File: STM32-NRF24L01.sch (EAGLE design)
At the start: 16 parts, among them IC1 STM32F030K6T6, IC2 MCP73811/2, J1 61301411121, J2 61301411121, P1 PUSH-SMD

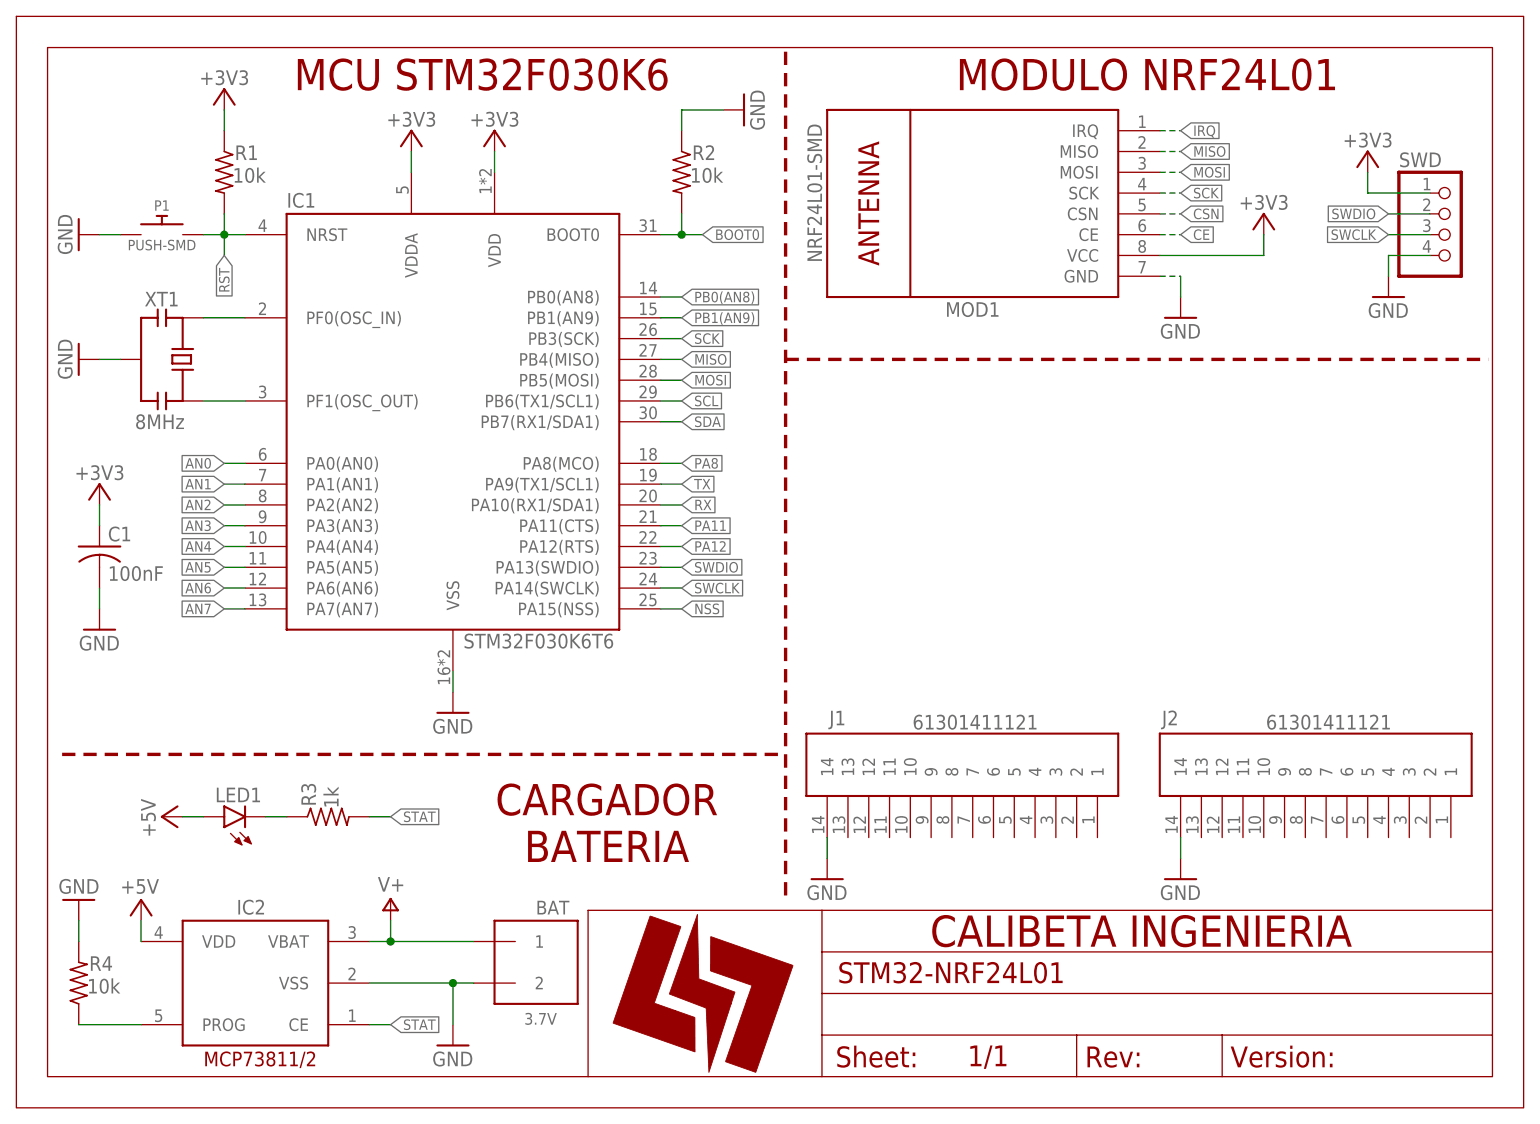
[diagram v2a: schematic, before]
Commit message: Add Regulador 3V3
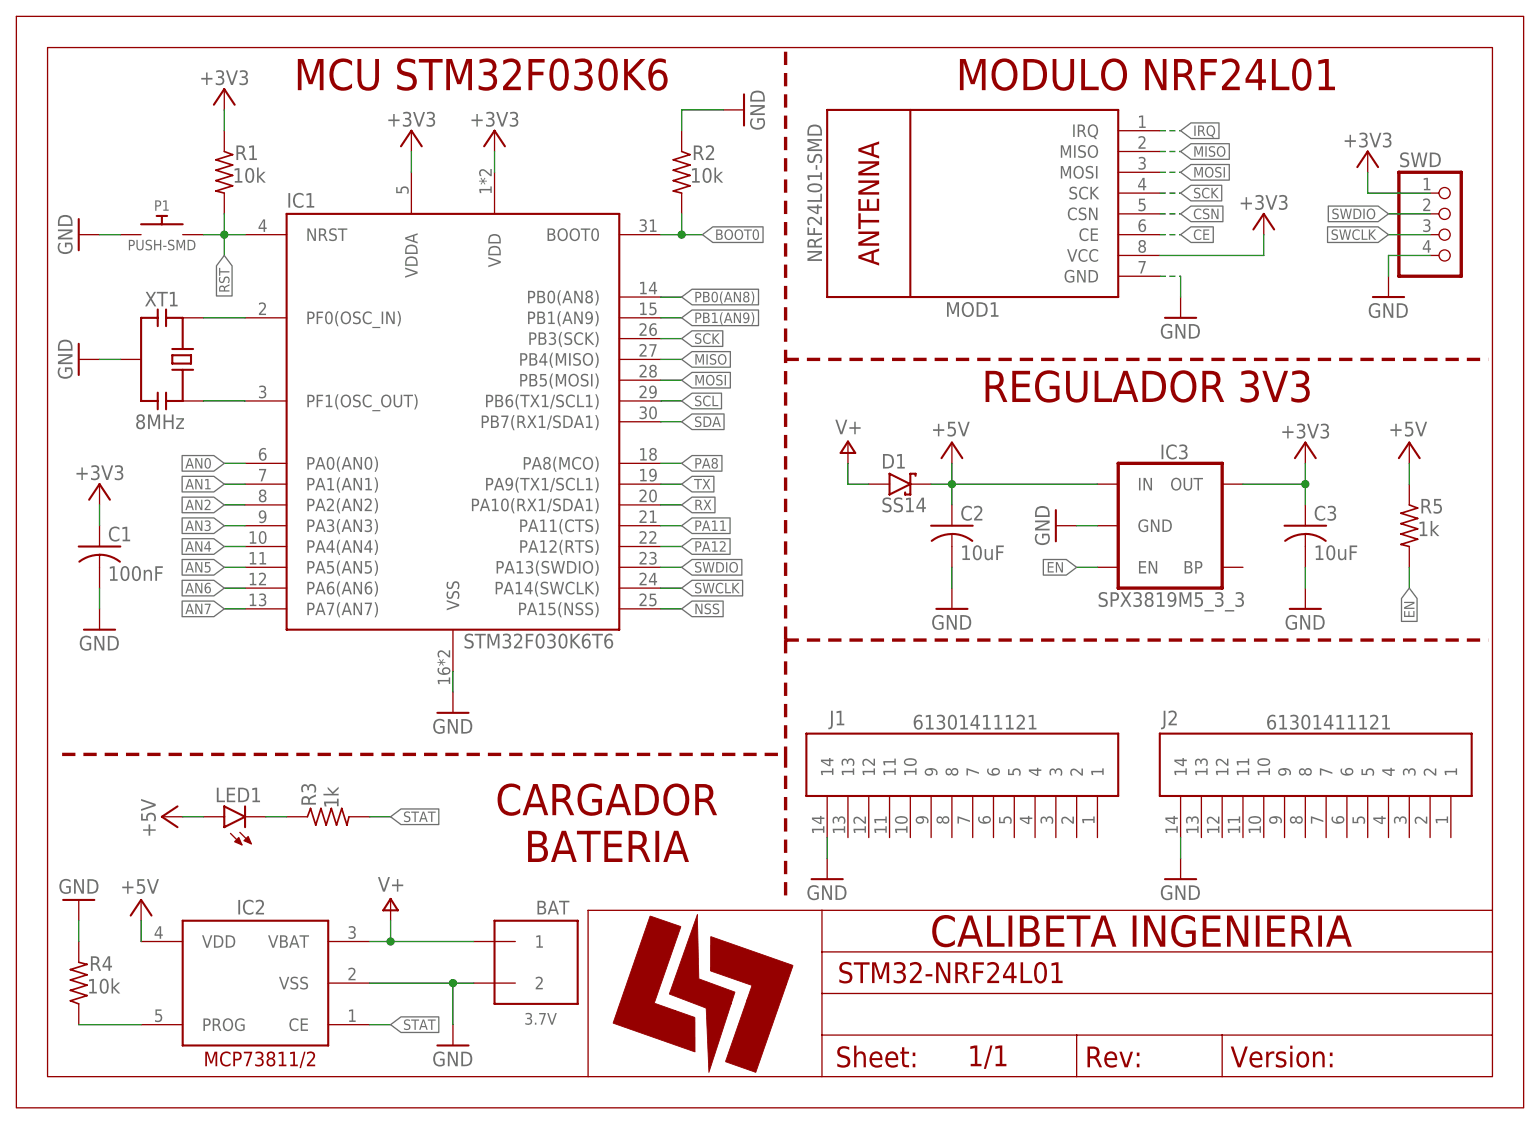
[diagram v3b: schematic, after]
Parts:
- added C2, C3: 10uF, CaliBeta-RCL:CAPC0805
- added D1: SS14, CaliBeta-Diodos:SS14
- added IC3: SPX3819M5_3_3, SparkFun-IC-Power:V_REG_SPX3819-SOT23-5
- added R5: 1k, CaliBeta-RCL:RESISTOR_R0805
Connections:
- new net EN: IC3.EN, R5.2
- net +3V3: now also C3.1, IC3.OUT
- net +5V: now also C2.1, D1.K, IC3.IN, R5.1
- net GND: now also C2.2, C3.2, IC3.GND
- net V+: now also D1.A
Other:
- note added: "REGULADOR 3V3"
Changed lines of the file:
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@@
 <part name="P+3" library="supply1" library_urn="urn:adsk.eagle:library:371" deviceset="V+" device=""/>
 <part name="GND10" library="supply1" library_urn="urn:adsk.eagle:library:371" deviceset="GND" device=""/>
+<part name="IC3" library="SparkFun-IC-Power" library_urn="urn:adsk.eagle:library:526" deviceset="V_REG_SPX3819" device="-SOT23-5" package3d_urn="urn:adsk.eagle:package:39060/1" value="SPX3819M5_3_3"/>
+<part name="D1" library="CaliBeta-Diodos" library_urn="urn:adsk.eagle:library:14345451" deviceset="SS14" device="" package3d_urn="urn:adsk.eagle:package:14345492/2"/>
+<part name="P+4" library="supply1" library_urn="urn:adsk.eagle:library:371" deviceset="V+" device=""/>
+<part name="P+5" library="supply1" library_urn="urn:adsk.eagle:library:371" deviceset="+5V" device=""/>
+<part name="C2" library="CaliBeta-RCL" library_urn="urn:adsk.eagle:library:14345719" deviceset="CAP" device="C0805" package3d_urn="urn:adsk.eagle:package:14345754/1" value="10uF"/>
+<part name="GND12" library="supply1" library_urn="urn:adsk.eagle:library:371" deviceset="GND" device=""/>
+<part name="+3V7" library="supply1" library_urn="urn:adsk.eagle:library:371" deviceset="+3V3" device=""/>
+<part name="C3" library="CaliBeta-RCL" library_urn="urn:adsk.eagle:library:14345719" deviceset="CAP" device="C0805" package3d_urn="urn:adsk.eagle:package:14345754/1" value="10uF"/>
+<part name="GND13" library="supply1" library_urn="urn:adsk.eagle:library:371" deviceset="GND" device=""/>
+<part name="GND14" library="supply1" library_urn="urn:adsk.eagle:library:371" deviceset="GND" device=""/>
+<part name="R5" library="CaliBeta-RCL" library_urn="urn:adsk.eagle:library:14345719" deviceset="RESISTOR_" device="R0805" package3d_urn="urn:adsk.eagle:package:14345749/1" value="1k"/>
+<part name="P+6" library="supply1" library_urn="urn:adsk.eagle:library:371" deviceset="+5V" device=""/>
 </parts>
 <sheets>
@@
 <plain>
 <text x="56.896" y="126.238" size="3.81" layer="94" ratio="10" align="center">MCU STM32F030K6</text>
-<wire x1="93.98" y1="129.032" x2="93.98" y2="43.18" width="0.4064" layer="94" style="longdash"/>
+<wire x1="93.98" y1="129.032" x2="93.98" y2="57.15" width="0.4064" layer="94" style="longdash"/>
 <text x="138.176" y="126.238" size="3.81" layer="94" ratio="10" align="center">MODULO NRF24L01</text>
+<wire x1="93.98" y1="57.15" x2="93.98" y2="43.18" width="0.4064" layer="94" style="longdash"/>
 <wire x1="93.98" y1="43.18" x2="93.98" y2="25.4" width="0.4064" layer="94" style="longdash"/>
 <wire x1="5.588" y1="43.18" x2="93.98" y2="43.18" width="0.4064" layer="94" style="longdash"/>
@@
 <text x="72.136" y="34.798" size="3.81" layer="94" ratio="10" align="center">CARGADOR
 BATERIA</text>
+<text x="138.176" y="88.138" size="3.81" layer="94" ratio="10" align="center">REGULADOR 3V3</text>
+<wire x1="93.98" y1="57.15" x2="179.832" y2="57.15" width="0.4064" layer="94" style="longdash"/>
 </plain>
 <instances>
@@
 <attribute name="VALUE" x="50.8" y="5.08" size="1.778" layer="96"/>
 </instance>
+<instance part="IC3" gate="G$1" x="142.24" y="71.12" smashed="yes">
+<attribute name="NAME" x="139.7" y="79.248" size="1.778" layer="95" font="vector"/>
+<attribute name="VALUE" x="132.08" y="62.992" size="1.778" layer="96" font="vector" align="top-left"/>
+</instance>
+<instance part="D1" gate="G$1" x="106.68" y="76.2" smashed="yes">
+<attribute name="NAME" x="105.664" y="78.105" size="1.778" layer="95"/>
+<attribute name="VALUE" x="105.664" y="72.771" size="1.778" layer="96"/>
+</instance>
+<instance part="P+4" gate="1" x="101.6" y="81.28" smashed="yes">
+<attribute name="VALUE" x="103.378" y="84.074" size="1.778" layer="96" rot="R180"/>
+</instance>
+<instance part="P+5" gate="1" x="114.3" y="81.28" smashed="yes">
+<attribute name="VALUE" x="111.76" y="82.042" size="1.778" layer="96"/>
+</instance>
+<instance part="C2" gate="G$1" x="114.3" y="71.12" smashed="yes">
+<attribute name="NAME" x="115.316" y="71.755" size="1.778" layer="95"/>
+<attribute name="VALUE" x="115.316" y="66.929" size="1.778" layer="96"/>
+</instance>
+<instance part="GND12" gate="1" x="114.3" y="60.96" smashed="yes">
+<attribute name="VALUE" x="111.76" y="58.42" size="1.778" layer="96"/>
+</instance>
+<instance part="+3V7" gate="G$1" x="157.48" y="81.28" smashed="yes">
+<attribute name="VALUE" x="154.432" y="81.788" size="1.778" layer="96"/>
+</instance>
+<instance part="C3" gate="G$1" x="157.48" y="71.12" smashed="yes">
+<attribute name="NAME" x="158.496" y="71.755" size="1.778" layer="95"/>
+<attribute name="VALUE" x="158.496" y="66.929" size="1.778" layer="96"/>
+</instance>
+<instance part="GND13" gate="1" x="157.48" y="60.96" smashed="yes">
+<attribute name="VALUE" x="154.94" y="58.42" size="1.778" layer="96"/>
+</instance>
+<instance part="GND14" gate="1" x="127" y="71.12" smashed="yes" rot="R270">
+<attribute name="VALUE" x="124.46" y="73.66" size="1.778" layer="96" rot="R270"/>
+</instance>
+<instance part="R5" gate="G$1" x="170.18" y="71.12" smashed="yes" rot="R270">
+<attribute name="NAME" x="171.45" y="72.6186" size="1.778" layer="95"/>
+<attribute name="VALUE" x="171.196" y="69.85" size="1.778" layer="96"/>
+</instance>
+<instance part="P+6" gate="1" x="170.18" y="81.28" smashed="yes">
+<attribute name="VALUE" x="167.64" y="82.042" size="1.778" layer="96"/>
+</instance>
 </instances>
 <busses>
@@
 <wire x1="48.26" y1="114.3" x2="48.26" y2="116.84" width="0.1524" layer="91"/>
 <pinref part="+3V6" gate="G$1" pin="+3V3"/>
+</segment>
+<segment>
+<pinref part="+3V7" gate="G$1" pin="+3V3"/>
+<pinref part="IC3" gate="G$1" pin="OUT"/>
+<wire x1="157.48" y1="78.74" x2="157.48" y2="76.2" width="0.1524" layer="91"/>
+<wire x1="157.48" y1="76.2" x2="149.86" y2="76.2" width="0.1524" layer="91"/>
+<pinref part="C3" gate="G$1" pin="1"/>
+<wire x1="157.48" y1="73.66" x2="157.48" y2="76.2" width="0.1524" layer="91"/>
+<junction x="157.48" y="76.2"/>
 </segment>
 </net>
@@
 <junction x="53.34" y="15.24"/>
 </segment>
+<segment>
+<pinref part="C2" gate="G$1" pin="2"/>
+<pinref part="GND12" gate="1" pin="GND"/>
+<wire x1="114.3" y1="63.5" x2="114.3" y2="66.04" width="0.1524" layer="91"/>
+</segment>
+<segment>
+<pinref part="C3" gate="G$1" pin="2"/>
+<pinref part="GND13" gate="1" pin="GND"/>
+<wire x1="157.48" y1="63.5" x2="157.48" y2="66.04" width="0.1524" layer="91"/>
+</segment>
+<segment>
+<pinref part="IC3" gate="G$1" pin="GND"/>
+<pinref part="GND14" gate="1" pin="GND"/>
+<wire x1="129.54" y1="71.12" x2="132.08" y2="71.12" width="0.1524" layer="91"/>
+</segment>
 </net>
 <net name="CE" class="0">
@@
 <pinref part="P+1" gate="1" pin="+5V"/>
 <wire x1="20.32" y1="35.56" x2="22.86" y2="35.56" width="0.1524" layer="91"/>
+</segment>
+<segment>
+<pinref part="P+5" gate="1" pin="+5V"/>
+<pinref part="D1" gate="G$1" pin="K"/>
+<wire x1="114.3" y1="78.74" x2="114.3" y2="76.2" width="0.1524" layer="91"/>
+<wire x1="114.3" y1="76.2" x2="111.76" y2="76.2" width="0.1524" layer="91"/>
+<pinref part="IC3" gate="G$1" pin="IN"/>
+<wire x1="132.08" y1="76.2" x2="114.3" y2="76.2" width="0.1524" layer="91"/>
+<junction x="114.3" y="76.2"/>
+<pinref part="C2" gate="G$1" pin="1"/>
+<wire x1="114.3" y1="73.66" x2="114.3" y2="76.2" width="0.1524" layer="91"/>
+</segment>
+<segment>
+<pinref part="R5" gate="G$1" pin="1"/>
+<pinref part="P+6" gate="1" pin="+5V"/>
+<wire x1="170.18" y1="78.74" x2="170.18" y2="76.2" width="0.1524" layer="91"/>
 </segment>
 </net>
@@
 <junction x="45.72" y="20.32"/>
 </segment>
+<segment>
+<pinref part="D1" gate="G$1" pin="A"/>
+<pinref part="P+4" gate="1" pin="V+"/>
+<wire x1="104.14" y1="76.2" x2="101.6" y2="76.2" width="0.1524" layer="91"/>
+<wire x1="101.6" y1="76.2" x2="101.6" y2="78.74" width="0.1524" layer="91"/>
+</segment>
 </net>
 <net name="STAT" class="0">
@@
 </segment>
 </net>
+<net name="EN" class="0">
+<segment>
+<pinref part="IC3" gate="G$1" pin="EN"/>
+<wire x1="132.08" y1="66.04" x2="129.54" y2="66.04" width="0.1524" layer="91"/>
+<label x="129.54" y="66.04" size="1.27" layer="95" ratio="10" rot="R180" xref="yes"/>
+</segment>
+<segment>
+<pinref part="R5" gate="G$1" pin="2"/>
+<wire x1="170.18" y1="66.04" x2="170.18" y2="63.5" width="0.1524" layer="91"/>
+<label x="170.18" y="63.5" size="1.27" layer="95" ratio="10" rot="R270" xref="yes"/>
+</segment>
+</net>

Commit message: Terminado SCH, Inicio BRD
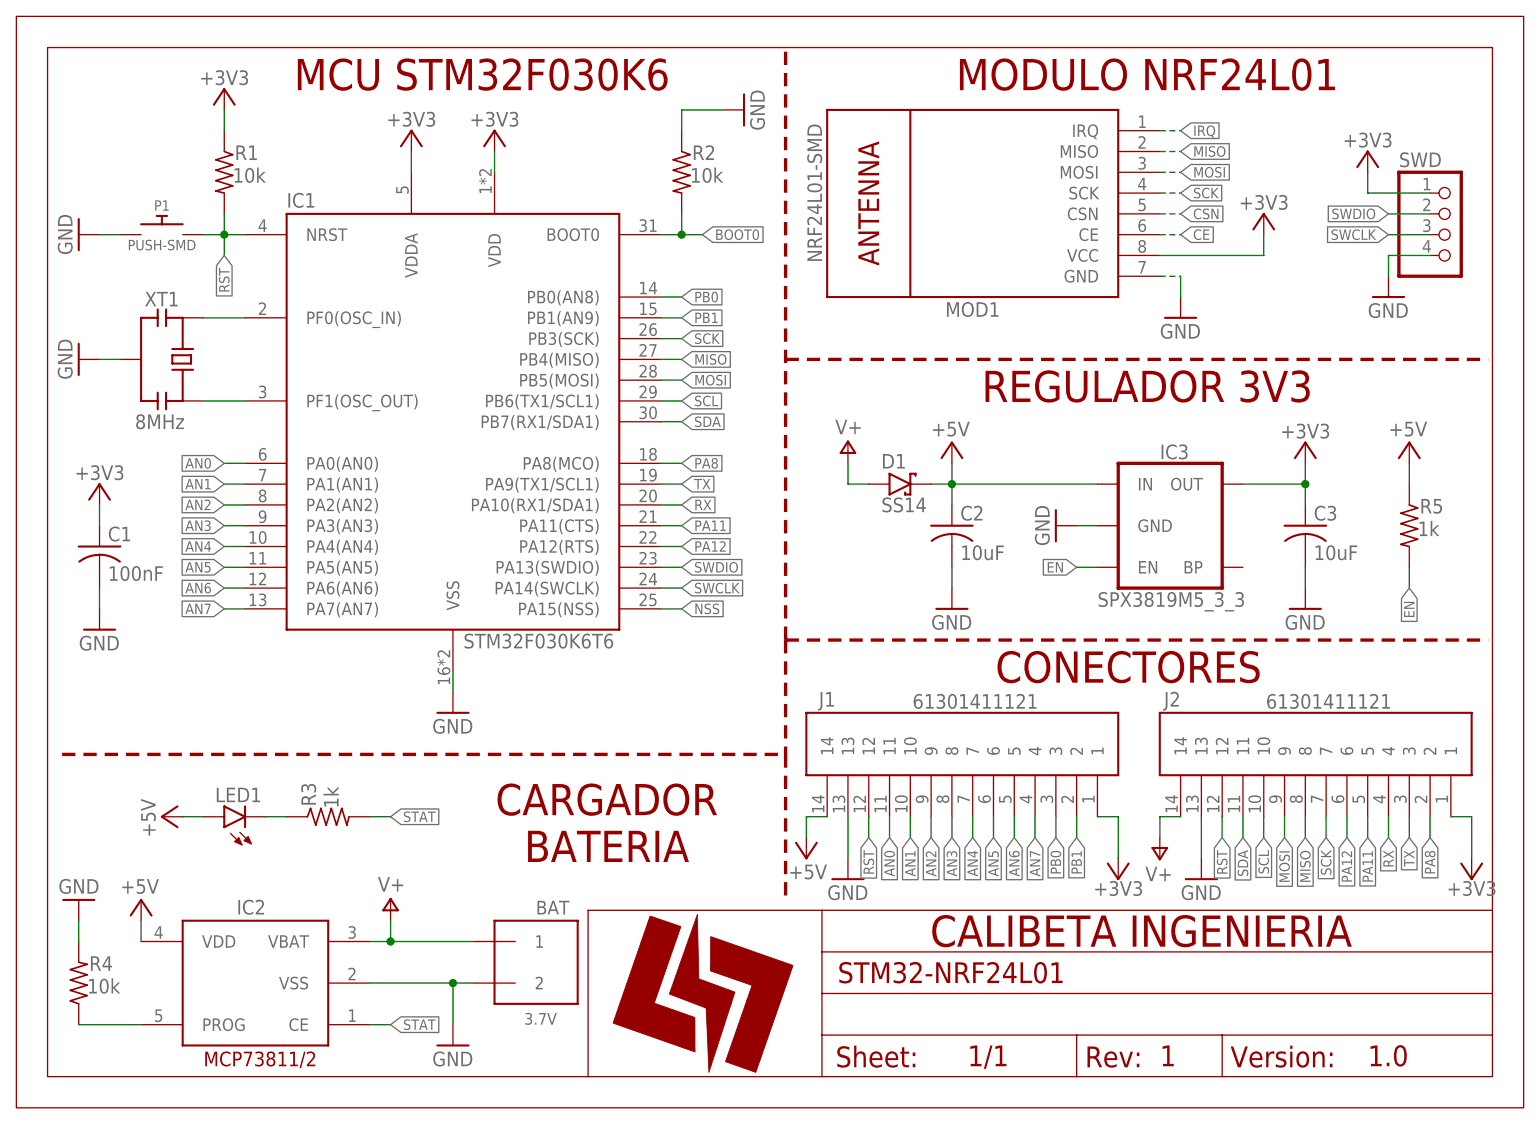
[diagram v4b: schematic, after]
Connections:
- removed net PB0(AN8): IC1.PB0(AN8)
- removed net PB1(AN9): IC1.PB1(AN9)
- new net PB0: IC1.PB0(AN8), J1.3
- new net PB1: IC1.PB1(AN9), J1.2
- net +3V3: now also J1.1, J2.1
- net +5V: now also J1.14
- net AN0: now also J1.11
- net AN1: now also J1.10
- net AN2: now also J1.9
- net AN3: now also J1.8
- net AN4: now also J1.7
- net AN5: now also J1.6
- net AN6: now also J1.5
- net AN7: now also J1.4
- net GND: now also J1.13, J2.13; no longer J1.14, J2.14
- net MISO: now also J2.8
- net MOSI: now also J2.9
- net PA11: now also J2.5
- net PA12: now also J2.6
- net PA8: now also J2.2
- net RST: now also J1.12, J2.12
- net RX: now also J2.4
- net SCK: now also J2.7
- net SCL: now also J2.10
- net SDA: now also J2.11
- net TX: now also J2.3
- net V+: now also J2.14
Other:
- note added: "1"
- note added: "1.0"
- note added: "CONECTORES"
- moved on the sheet: J1, J2
